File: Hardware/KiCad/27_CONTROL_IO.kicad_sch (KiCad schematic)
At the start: 0 parts

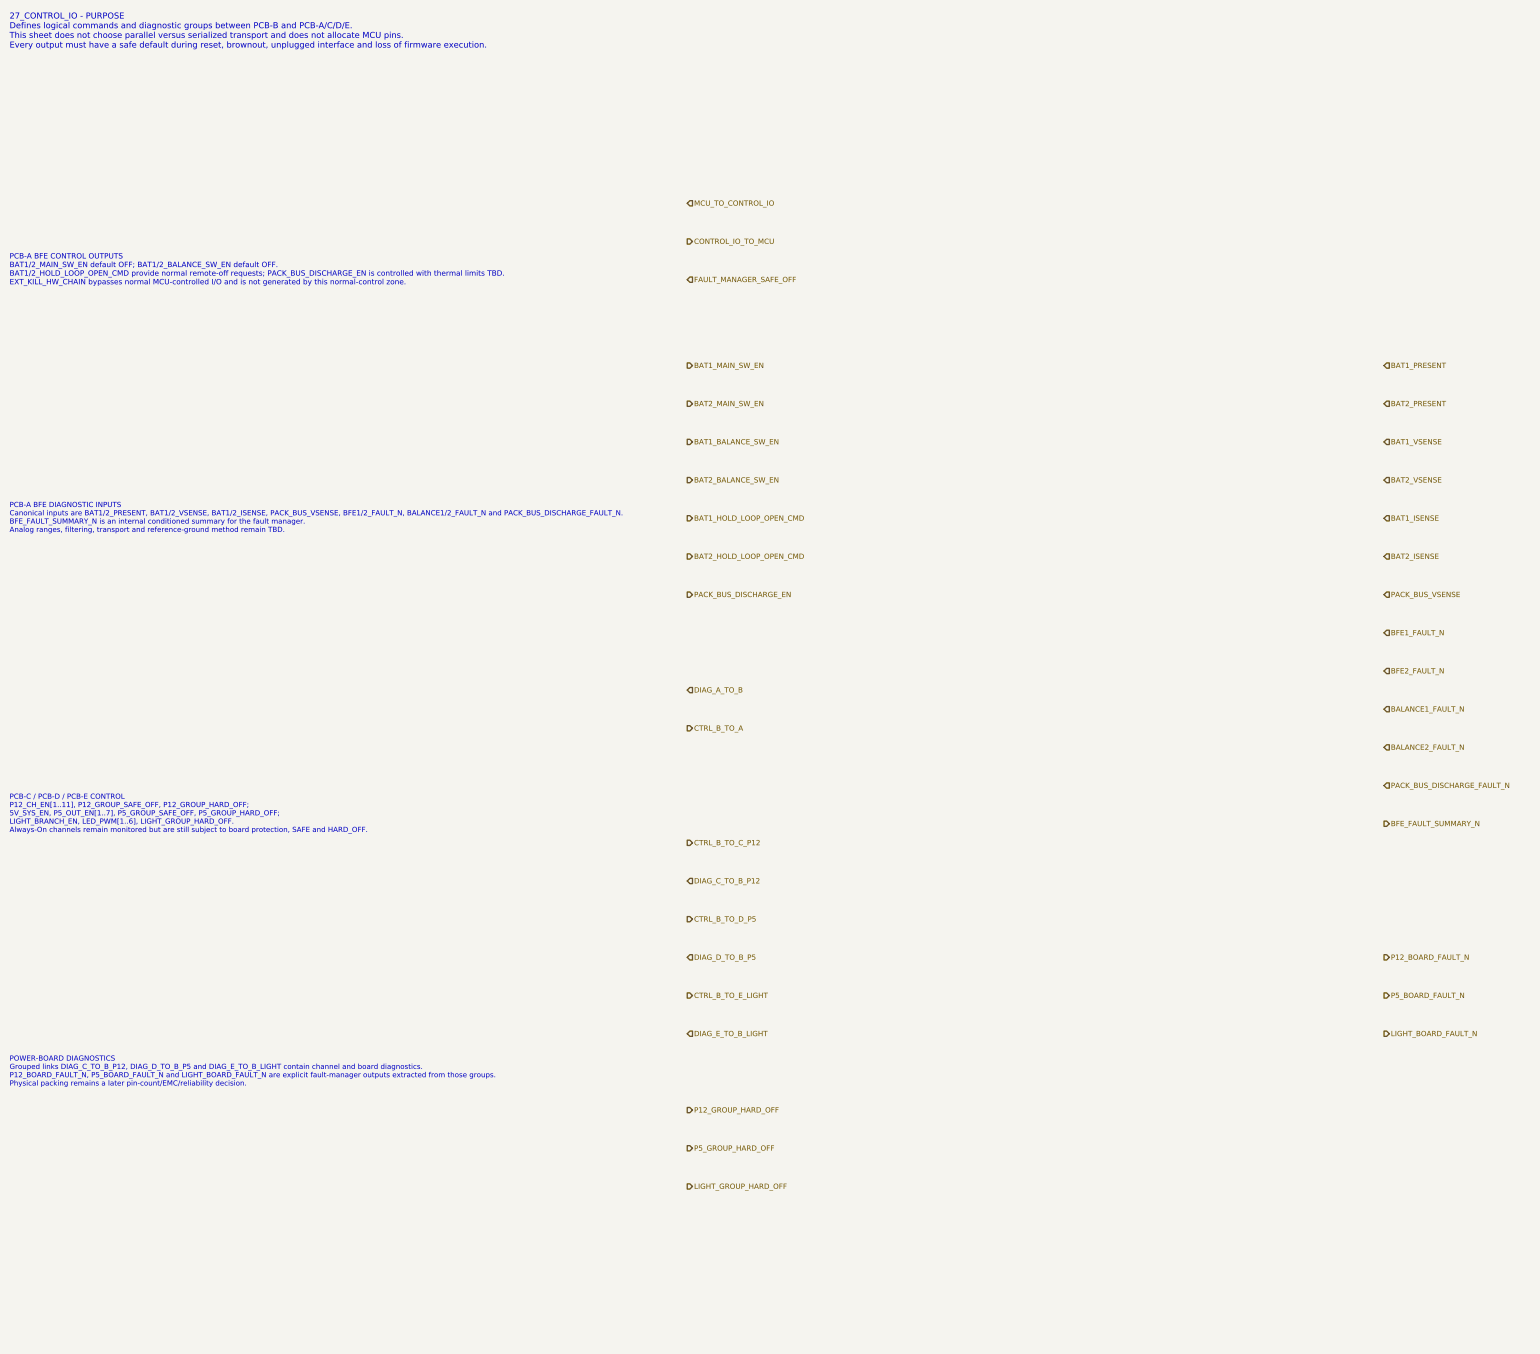
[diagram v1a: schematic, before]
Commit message: hardware: align PCB-C POWER_12V interfaces
Merge PCB-C interface consistency after verifying exact control/diagnostic buses and SAFE/HARD_OFF semantics.
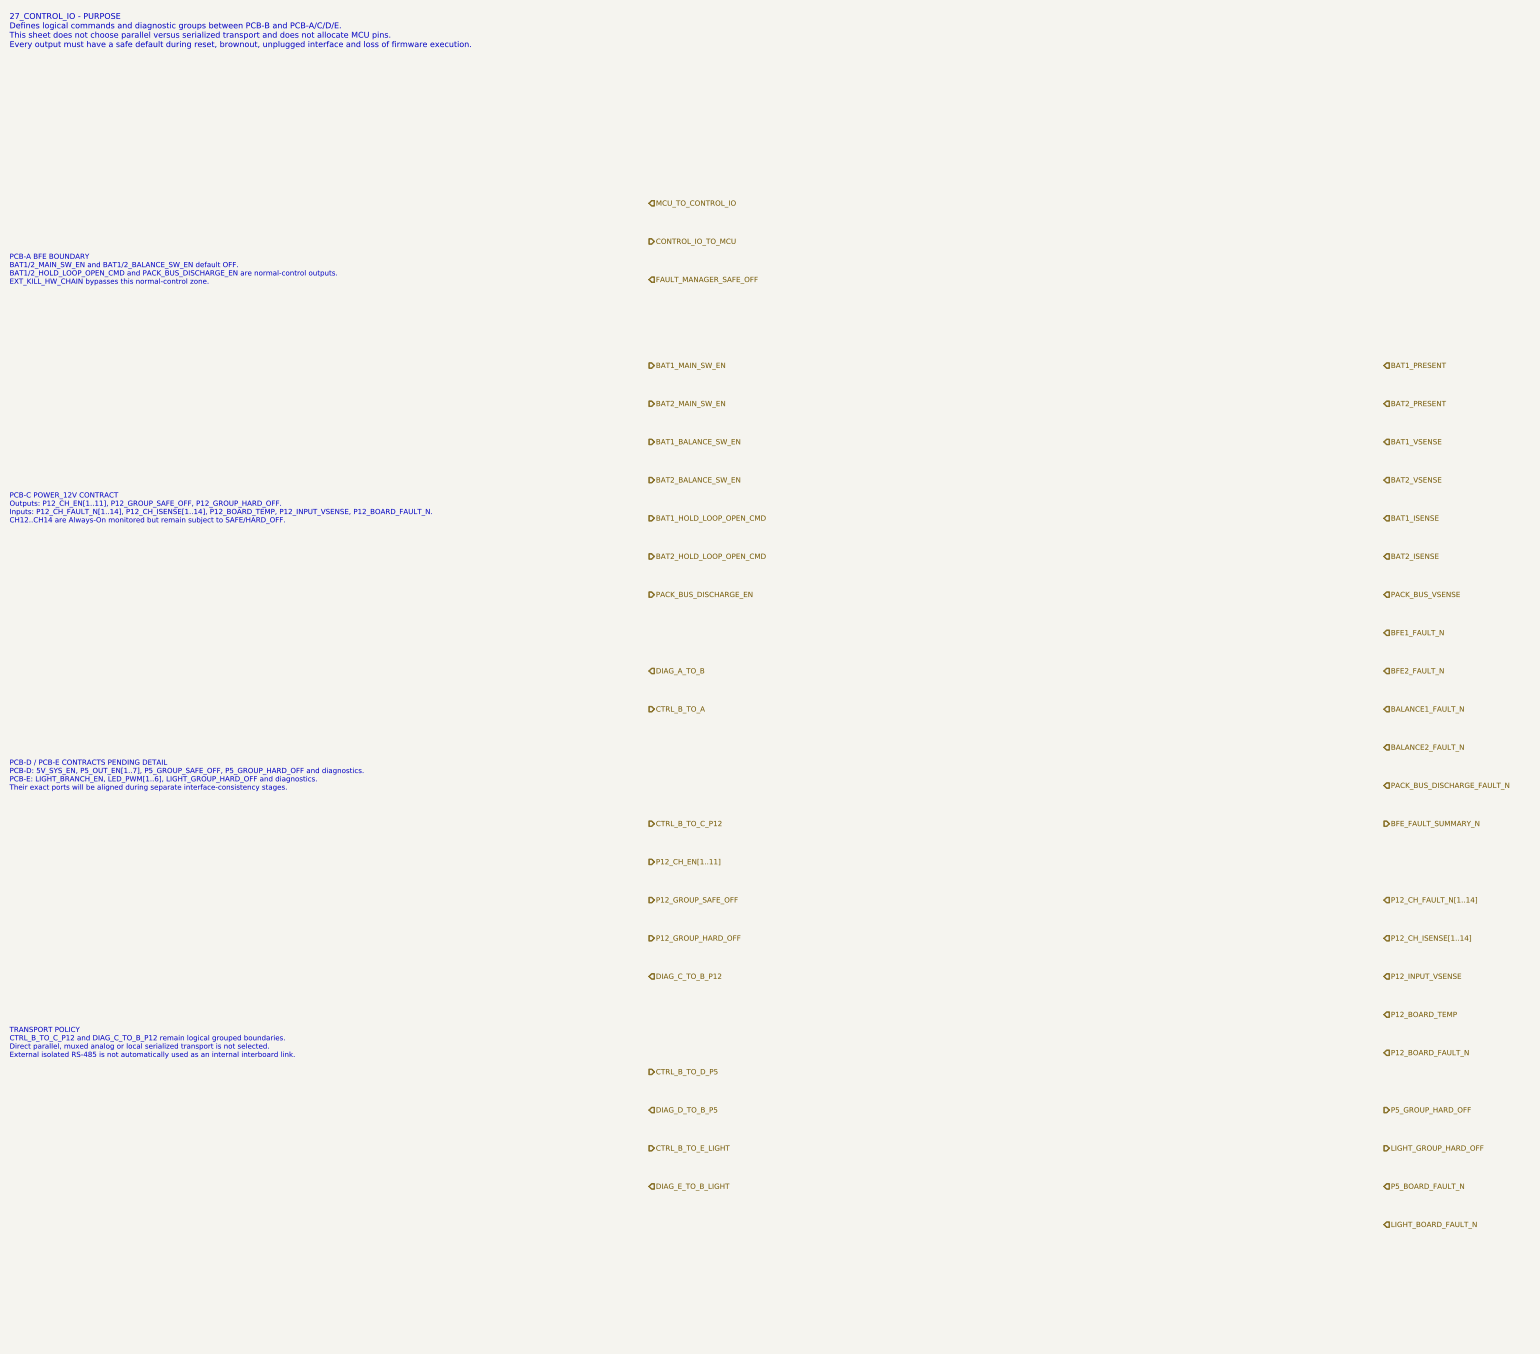
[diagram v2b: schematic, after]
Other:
- note added: "PCB-A BFE BOUNDARY BAT1/2_MAIN_SW_EN and BAT1/2_BALANCE_SW_EN default OFF. BAT1/2_HOLD_LOOP_OPEN_CMD and PACK_BUS_DISCHARGE_EN are normal-control outputs. EXT_KILL_HW_CHAIN bypasses this normal-control zone."
- note added: "PCB-C POWER_12V CONTRACT Outputs: P12_CH_EN[1..11], P12_GROUP_SAFE_OFF, P12_GROUP_HARD_OFF. Inputs: P12_CH_FAULT_N[1..14], P12_CH_ISENSE[1..14], P12_BOARD_TEMP, P12_INPUT_VSENSE, P12_BOARD_FAULT_N. CH12..CH14 are Always-On monitored but remain subject to SAFE/HARD_OFF."
- note added: "PCB-D / PCB-E CONTRACTS PENDING DETAIL PCB-D: 5V_SYS_EN, P5_OUT_EN[1..7], P5_GROUP_SAFE_OFF, P5_GROUP_HARD_OFF and diagnostics. PCB-E: LIGHT_BRANCH_EN, LED_PWM[1..6], LIGHT_GROUP_HARD_OFF and diagnostics. Their exact ports will be aligned during separate interface-consistency stages."
- note added: "TRANSPORT POLICY CTRL_B_TO_C_P12 and DIAG_C_TO_B_P12 remain logical grouped boundaries. Direct parallel, muxed analog or local serialized transport is not selected. External isolated RS-485 is not automatically used as an internal interboard link."
- note removed: "PCB-A BFE CONTROL OUTPUTS BAT1/2_MAIN_SW_EN default OFF; BAT1/2_BALANCE_SW_EN default OFF. BAT1/2_HOLD_LOOP_OPEN_CMD provide normal remote-off requests; PACK_BUS_DISCHARGE_EN is controlled with thermal limits TBD. EXT_KILL_HW_CHAIN bypasses normal MCU-controlled I/O and is not generated by this normal-control zone."
- note removed: "PCB-A BFE DIAGNOSTIC INPUTS Canonical inputs are BAT1/2_PRESENT, BAT1/2_VSENSE, BAT1/2_ISENSE, PACK_BUS_VSENSE, BFE1/2_FAULT_N, BALANCE1/2_FAULT_N and PACK_BUS_DISCHARGE_FAULT_N. BFE_FAULT_SUMMARY_N is an internal conditioned summary for the fault manager. Analog ranges, filtering, transport and reference-ground method remain TBD."
- note removed: "PCB-C / PCB-D / PCB-E CONTROL P12_CH_EN[1..11], P12_GROUP_SAFE_OFF, P12_GROUP_HARD_OFF; 5V_SYS_EN, P5_OUT_EN[1..7], P5_GROUP_SAFE_OFF, P5_GROUP_HARD_OFF; LIGHT_BRANCH_EN, LED_PWM[1..6], LIGHT_GROUP_HARD_OFF. Always-On channels remain monitored but are still subject to board protection, SAFE and HARD_OFF."
- note removed: "POWER-BOARD DIAGNOSTICS Grouped links DIAG_C_TO_B_P12, DIAG_D_TO_B_P5 and DIAG_E_TO_B_LIGHT contain channel and board diagnostics. P12_BOARD_FAULT_N, P5_BOARD_FAULT_N and LIGHT_BOARD_FAULT_N are explicit fault-manager outputs extracted from those groups. Physical packing remains a later pin-count/EMC/reliability decision."

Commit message: hardware: align PCB-D POWER_5V interfaces
Merge PCB-D interface consistency after verifying exact control/diagnostic buses and separation from critical power.
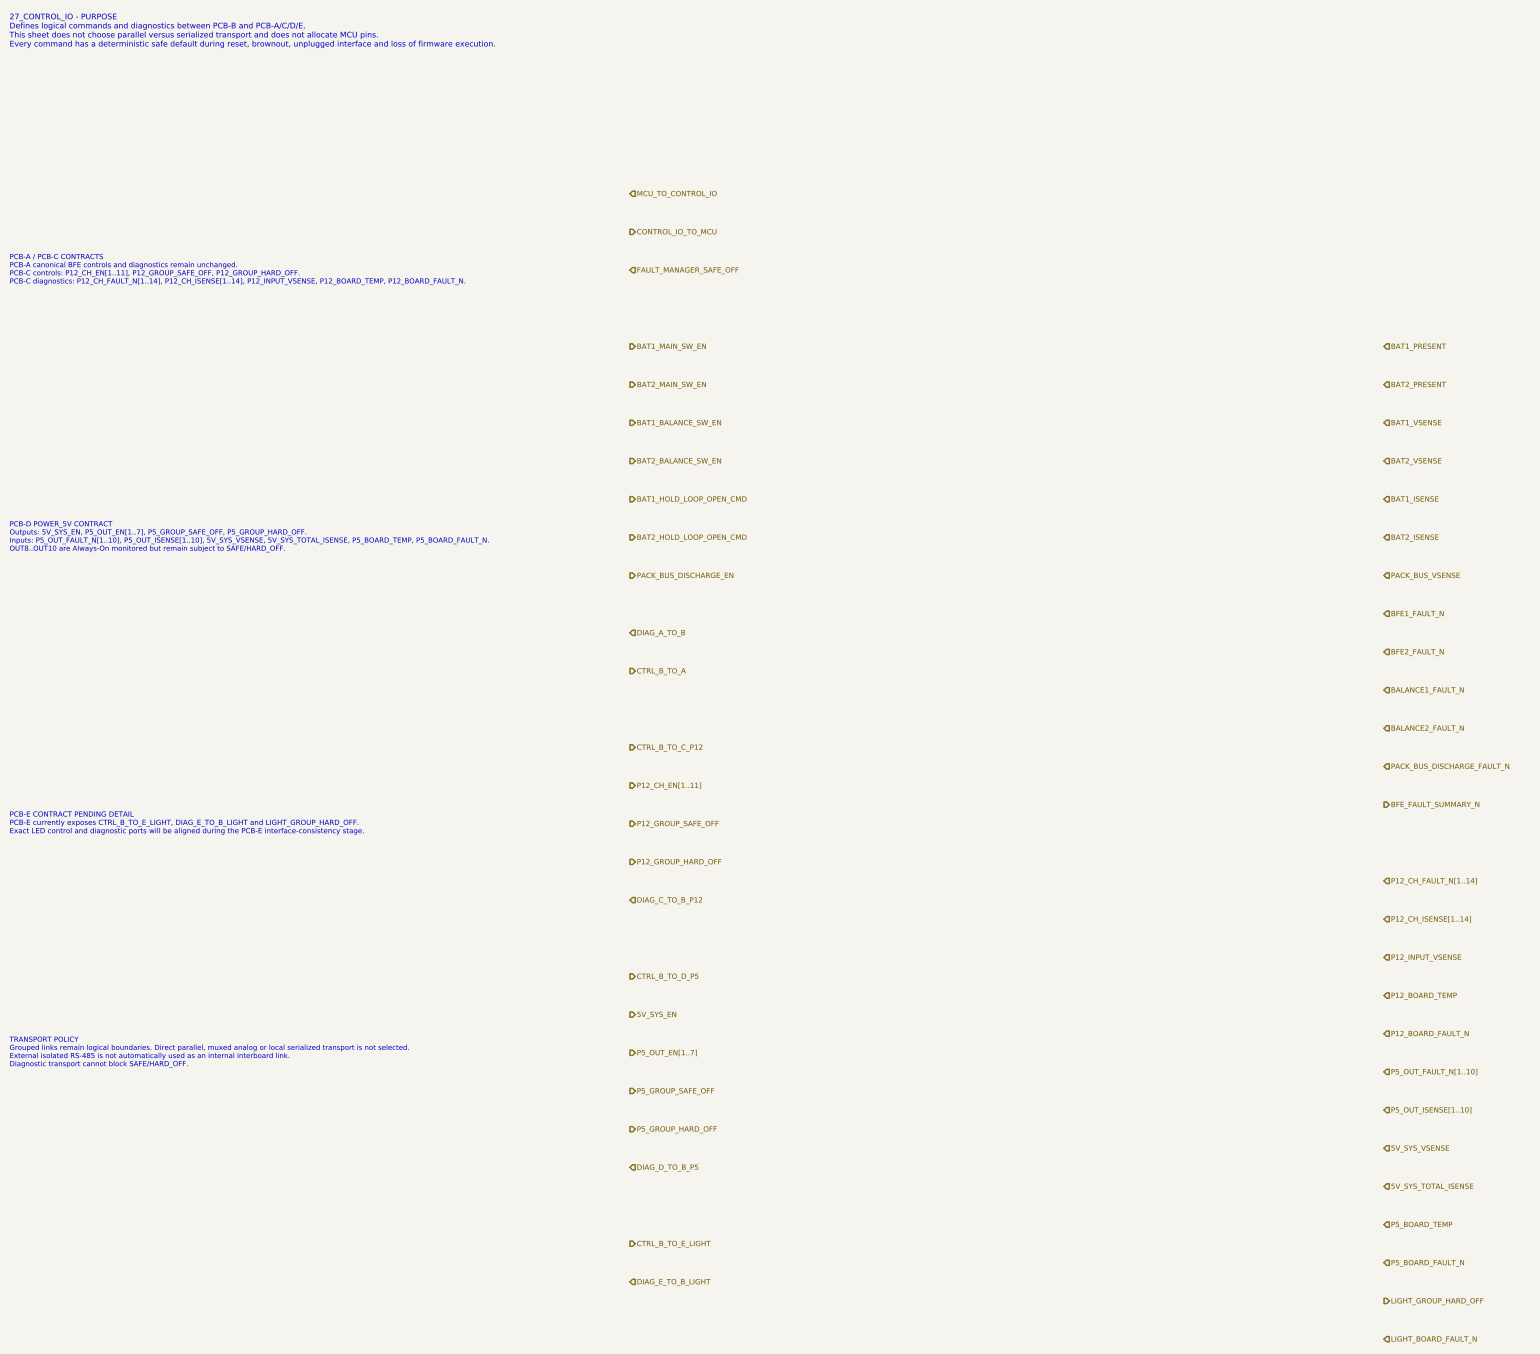
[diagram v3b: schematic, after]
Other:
- note added: "27_CONTROL_IO - PURPOSE Defines logical commands and diagnostics between PCB-B and PCB-A/C/D/E. This sheet does not choose parallel versus serialized transport and does not allocate MCU pins. Every command has a deterministic safe default during reset, brownout, unplugged interface and loss of firmware execution."
- note added: "PCB-A / PCB-C CONTRACTS PCB-A canonical BFE controls and diagnostics remain unchanged. PCB-C controls: P12_CH_EN[1..11], P12_GROUP_SAFE_OFF, P12_GROUP_HARD_OFF. PCB-C diagnostics: P12_CH_FAULT_N[1..14], P12_CH_ISENSE[1..14], P12_INPUT_VSENSE, P12_BOARD_TEMP, P12_BOARD_FAULT_N."
- note added: "PCB-D POWER_5V CONTRACT Outputs: 5V_SYS_EN, P5_OUT_EN[1..7], P5_GROUP_SAFE_OFF, P5_GROUP_HARD_OFF. Inputs: P5_OUT_FAULT_N[1..10], P5_OUT_ISENSE[1..10], 5V_SYS_VSENSE, 5V_SYS_TOTAL_ISENSE, P5_BOARD_TEMP, P5_BOARD_FAULT_N. OUT8..OUT10 are Always-On monitored but remain subject to SAFE/HARD_OFF."
- note added: "PCB-E CONTRACT PENDING DETAIL PCB-E currently exposes CTRL_B_TO_E_LIGHT, DIAG_E_TO_B_LIGHT and LIGHT_GROUP_HARD_OFF. Exact LED control and diagnostic ports will be aligned during the PCB-E interface-consistency stage."
- note added: "TRANSPORT POLICY Grouped links remain logical boundaries. Direct parallel, muxed analog or local serialized transport is not selected. External isolated RS-485 is not automatically used as an internal interboard link. Diagnostic transport cannot block SAFE/HARD_OFF."
- note removed: "27_CONTROL_IO - PURPOSE Defines logical commands and diagnostic groups between PCB-B and PCB-A/C/D/E. This sheet does not choose parallel versus serialized transport and does not allocate MCU pins. Every output must have a safe default during reset, brownout, unplugged interface and loss of firmware execution."
- note removed: "PCB-A BFE BOUNDARY BAT1/2_MAIN_SW_EN and BAT1/2_BALANCE_SW_EN default OFF. BAT1/2_HOLD_LOOP_OPEN_CMD and PACK_BUS_DISCHARGE_EN are normal-control outputs. EXT_KILL_HW_CHAIN bypasses this normal-control zone."
- note removed: "PCB-C POWER_12V CONTRACT Outputs: P12_CH_EN[1..11], P12_GROUP_SAFE_OFF, P12_GROUP_HARD_OFF. Inputs: P12_CH_FAULT_N[1..14], P12_CH_ISENSE[1..14], P12_BOARD_TEMP, P12_INPUT_VSENSE, P12_BOARD_FAULT_N. CH12..CH14 are Always-On monitored but remain subject to SAFE/HARD_OFF."
- note removed: "PCB-D / PCB-E CONTRACTS PENDING DETAIL PCB-D: 5V_SYS_EN, P5_OUT_EN[1..7], P5_GROUP_SAFE_OFF, P5_GROUP_HARD_OFF and diagnostics. PCB-E: LIGHT_BRANCH_EN, LED_PWM[1..6], LIGHT_GROUP_HARD_OFF and diagnostics. Their exact ports will be aligned during separate interface-consistency stages."
- note removed: "TRANSPORT POLICY CTRL_B_TO_C_P12 and DIAG_C_TO_B_P12 remain logical grouped boundaries. Direct parallel, muxed analog or local serialized transport is not selected. External isolated RS-485 is not automatically used as an internal interboard link."
